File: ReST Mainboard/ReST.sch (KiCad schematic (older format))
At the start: 97 parts, among them IC1 AT24C128, P1 CONN_02X08, P10 CONN_01X04, P11 CONN_01X04, P12 CONN_02X04, P13 CONN_01X03, P14 CONN_02X03, P15 CONN_01X05, P16 CONN_01X03, P17 CONN_01X04, P18 CONN_02X04, P19 CONN_01X04, P2 CONN_02X08, P20 CONN_02X04, P21 CONN_02X04, P22 CONN_01X03, P23 SCREW_01X03, P24 CONN_01X03, P25 SCREW_01X03, P26 CONN_01X03, P27 SCREW_01X03, P28 CONN_01X03, P29 SCREW_01X03, P3 CONN_02X07, P30 CONN_01X03, P31 SCREW_01X03, P32 CONN_01X03, P33 SCREW_01X03, P34 CONN_01X03, P35 SCREW_01X04, P36 SCREW_01X04, P37 SCREW_01X04, P38 SCREW_01X04, P39 CONN_02X04, P4 CONN_02X10, P40 CONN_01X04, P41 CONN_01X04, P42 CONN_01X04, P43 CONN_02X03, P44 CONN_02X03, P45 CONN_02X03, P46 CONN_02X03, P5 USB_OTG, P6 CONN_02X05, P7 CONN_02X05, P8 CONN_01X09, P9 CONN_01X02, SW1 SW-SPST-NO, U1 STM32F103VE, U2 USBLC6-2, U3 L7805ACD2T-TR, U4 LM2574N-ADJ, U5 POLOLU_A4988, U6 POLOLU_A4988, U7 POLOLU_A4988, U8 POLOLU_A4988, X1 8MHZ RESONATOR

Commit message: Added BOM and changed Oscillator to Crystal
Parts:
- removed R4: 47R, Resistors_SMD:R_0805_HandSoldering, symbol R_Small
- removed X1: 8MHZ RESONATOR, ReST-Library:SMD-3P, symbol CRYSTAL_SMD
- added C24, C25: 30pF, Resistors_SMD:R_0805_HandSoldering, symbol C_Small
- added X1: Crystal_Small, Crystals:Crystal_HC49-SD_SMD, symbol Crystal_Small
- C8: footprint ok-polcaps-panasonic:CP-PANASONIC-SMT_C -> Capacitors_SMD:C_0805_HandSoldering
- C9: value 10nF -> 100nF
- L1: footprint ok-smd-generic:1206 -> Capacitors_SMD:C_0805_HandSoldering
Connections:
- wire segments 454 -> 447
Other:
- moved on the sheet: C8, C9, L1

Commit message: Removed unnecessary Libs and finished SD Card Module
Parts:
- U1: footprint ok-ic-smd:LQFP100-14x14 -> Housings_QFP:TQFP-100_14x14mm_Pitch0.5mm
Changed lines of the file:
@@
 F 0 "U1" H 2150 9550 50  0000 C CNN
 F 1 "STM32F103VE" H 4650 3950 50  0000 C CNN
-F 2 "ok-ic-smd:LQFP100-14x14" H 3500 6750 50  0001 C CNN
+F 2 "Housings_QFP:TQFP-100_14x14mm_Pitch0.5mm" H 3500 6750 50  0001 C CNN
 F 3 "" H 3500 7900 50  0000 C CNN
 	1    3500 6750

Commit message: Finally removed all unnecessary Libs and added Heatsink for 5V Regulator
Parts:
- C10: footprint ok-polcaps-panasonic:CP-PANASONIC-SMT_C -> ReST-Library:CP-PANASONIC-SMT_C
- C11, C12, C13: footprint ok-polcaps-panasonic:CP-PANASONIC-SMT_D -> ReST-Library:CP-PANASONIC-SMT_D
- C20, C21, C22, C23: footprint ok-polcaps-panasonic:CP-PANASONIC-SMT_D8 -> ReST-Library:CP-PANASONIC-SMT_D8
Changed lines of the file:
@@
 LIBS:dc-dc
 LIBS:diode
-LIBS:dp_devices
 LIBS:elec-unifil
 LIBS:ESD_Protection
@@
 LIBS:nordicsemi
 LIBS:nxp_armmcu
-LIBS:ok-74logic
-LIBS:ok-con-generic
-LIBS:ok-diodes
-LIBS:ok-generic
-LIBS:ok-ic-analog
-LIBS:ok-ic-atmel
-LIBS:ok-ic-com
-LIBS:ok-ic-memory
-LIBS:ok-ic-power
-LIBS:ok-ic-special
-LIBS:ok-ic-stm32
-LIBS:ok-jacks
-LIBS:ok-opto
-LIBS:ok-power
-LIBS:ok-relay
-LIBS:ok-switches
-LIBS:ok-transformers
-LIBS:ok-transistors
 LIBS:onsemi
 LIBS:Oscillators
-LIBS:pololu_a4988
 LIBS:Power_Management
 LIBS:powerint
@@
 LIBS:ReST-cache
 LIBS:STM32F103ZET6
-LIBS:small_rack-cache
 EELAYER 25 0
 EELAYER END
@@
 F 0 "C20" H 11760 3520 50  0000 L CNN
 F 1 "100uF" H 11760 3370 50  0000 L CNN
-F 2 "ok-polcaps-panasonic:CP-PANASONIC-SMT_D8" H 11750 3450 50  0001 C CNN
+F 2 "ReST-Library:CP-PANASONIC-SMT_D8" H 11750 3450 50  0001 C CNN
 F 3 "" H 11750 3450 50  0000 C CNN
 	1    11750 3450
@@
 F 0 "C21" H 11760 5520 50  0000 L CNN
 F 1 "100uF" H 11760 5370 50  0000 L CNN
-F 2 "ok-polcaps-panasonic:CP-PANASONIC-SMT_D8" H 11750 5450 50  0001 C CNN
+F 2 "ReST-Library:CP-PANASONIC-SMT_D8" H 11750 5450 50  0001 C CNN
 F 3 "" H 11750 5450 50  0000 C CNN
 	1    11750 5450
@@
 F 0 "C22" H 11810 9120 50  0000 L CNN
 F 1 "100uF" H 11810 8970 50  0000 L CNN
-F 2 "ok-polcaps-panasonic:CP-PANASONIC-SMT_D8" H 11800 9050 50  0001 C CNN
+F 2 "ReST-Library:CP-PANASONIC-SMT_D8" H 11800 9050 50  0001 C CNN
 F 3 "" H 11800 9050 50  0000 C CNN
 	1    11800 9050
@@
 F 0 "C23" H 11810 7420 50  0000 L CNN
 F 1 "100uF" H 11810 7270 50  0000 L CNN
-F 2 "ok-polcaps-panasonic:CP-PANASONIC-SMT_D8" H 11800 7350 50  0001 C CNN
+F 2 "ReST-Library:CP-PANASONIC-SMT_D8" H 11800 7350 50  0001 C CNN
 F 3 "" H 11800 7350 50  0000 C CNN
 	1    11800 7350
@@
 F 0 "C10" H 960 1770 50  0000 L CNN
 F 1 "10uF" H 960 1620 50  0000 L CNN
-F 2 "ok-polcaps-panasonic:CP-PANASONIC-SMT_C" H 950 1700 50  0001 C CNN
+F 2 "ReST-Library:CP-PANASONIC-SMT_C" H 950 1700 50  0001 C CNN
 F 3 "" H 950 1700 50  0000 C CNN
 	1    950  1700
@@
 F 0 "C11" H 1960 1770 50  0000 L CNN
 F 1 "22uF" H 1960 1620 50  0000 L CNN
-F 2 "ok-polcaps-panasonic:CP-PANASONIC-SMT_D" H 1950 1700 50  0001 C CNN
+F 2 "ReST-Library:CP-PANASONIC-SMT_D" H 1950 1700 50  0001 C CNN
 F 3 "" H 1950 1700 50  0000 C CNN
 	1    1950 1700
@@
 F 0 "C12" H 2560 1520 50  0000 L CNN
 F 1 "22uF" H 2560 1370 50  0000 L CNN
-F 2 "ok-polcaps-panasonic:CP-PANASONIC-SMT_D" H 2550 1450 50  0001 C CNN
+F 2 "ReST-Library:CP-PANASONIC-SMT_D" H 2550 1450 50  0001 C CNN
 F 3 "" H 2550 1450 50  0000 C CNN
 	1    2550 1450
@@
 F 0 "C13" H 4560 1770 50  0000 L CNN
 F 1 "220uF" H 4560 1620 50  0000 L CNN
-F 2 "ok-polcaps-panasonic:CP-PANASONIC-SMT_D" H 4550 1700 50  0001 C CNN
+F 2 "ReST-Library:CP-PANASONIC-SMT_D" H 4550 1700 50  0001 C CNN
 F 3 "" H 4550 1700 50  0000 C CNN
 	1    4550 1700

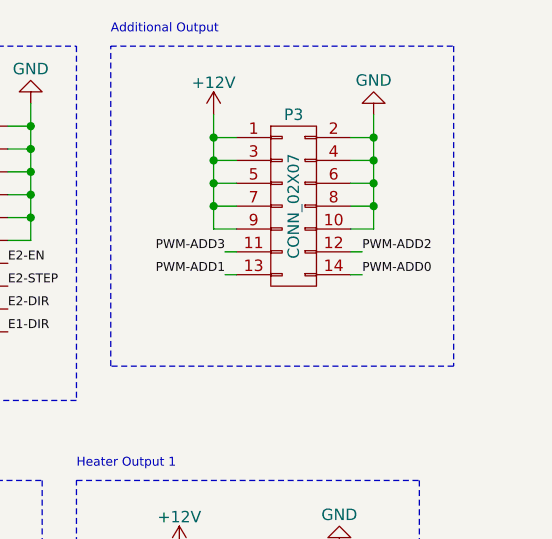
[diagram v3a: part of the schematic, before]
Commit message: Added IRLML2502 Module and added Ground vias everywhere
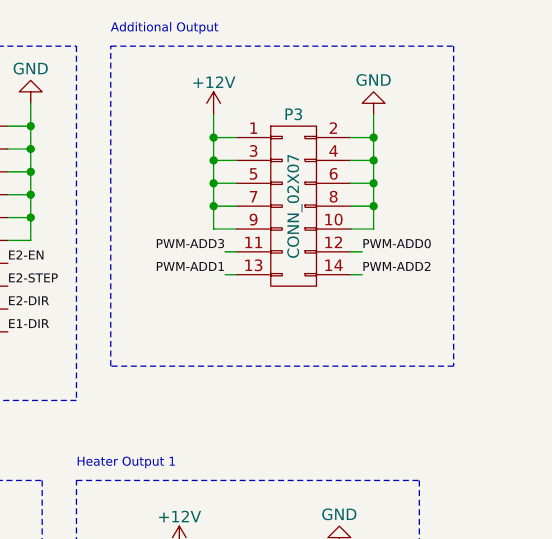
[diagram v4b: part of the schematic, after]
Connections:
- net PWM-ADD0: now also P3.12 (P12); no longer P3.14 (P14)
- net PWM-ADD2: now also P3.14 (P14); no longer P3.12 (P12)
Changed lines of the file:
@@
 Text Label 5700 6750 0    39   ~ 0
 I2C-SDA
+Text Label 15200 1550 0    39   ~ 0
+PWM-ADD0
 Text Label 15200 1650 0    39   ~ 0
-PWM-ADD0
-Text Label 15200 1550 0    39   ~ 0
 PWM-ADD2
 Text Label 14600 1550 2    39   ~ 0

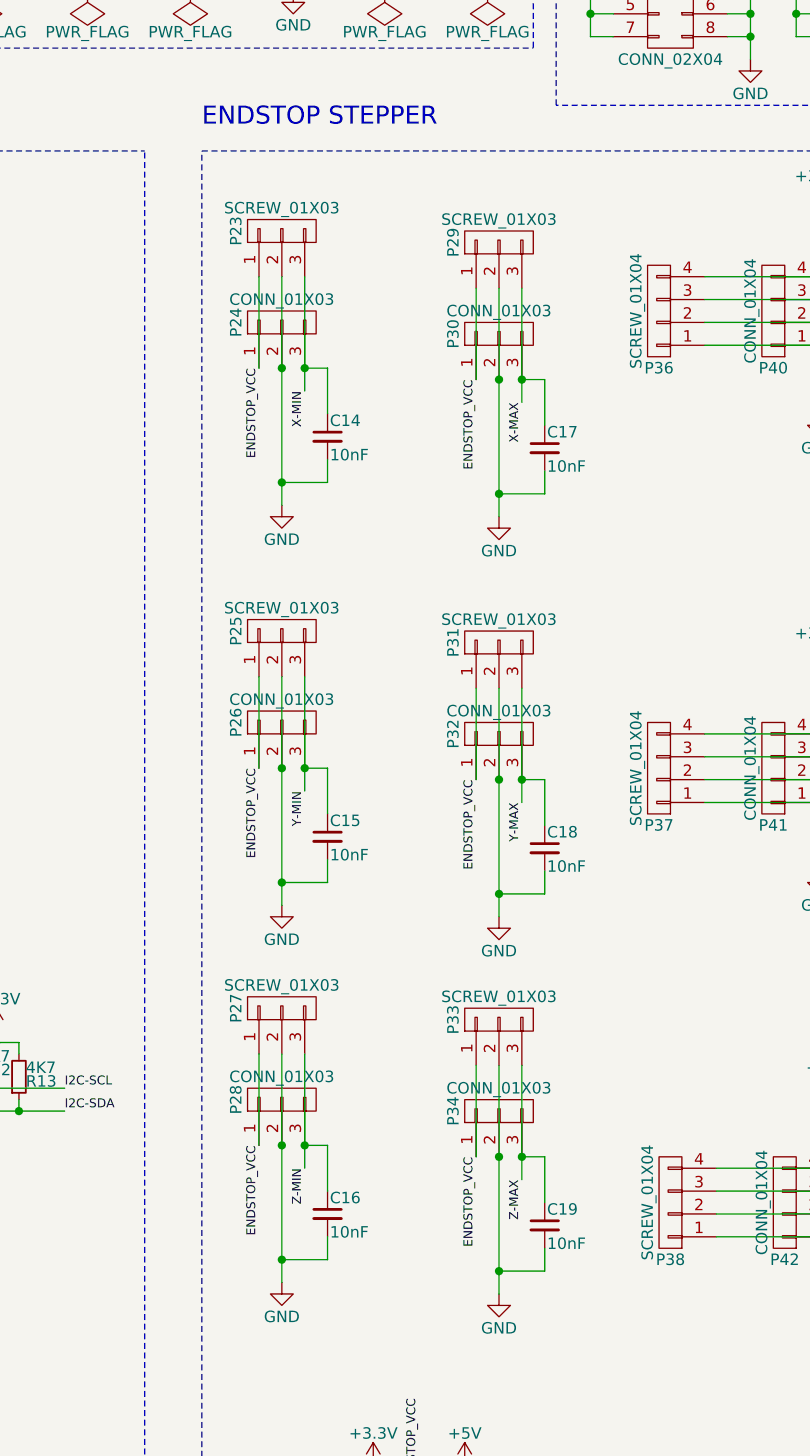
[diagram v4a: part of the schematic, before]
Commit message: Added BOM for all Items + suggested Links
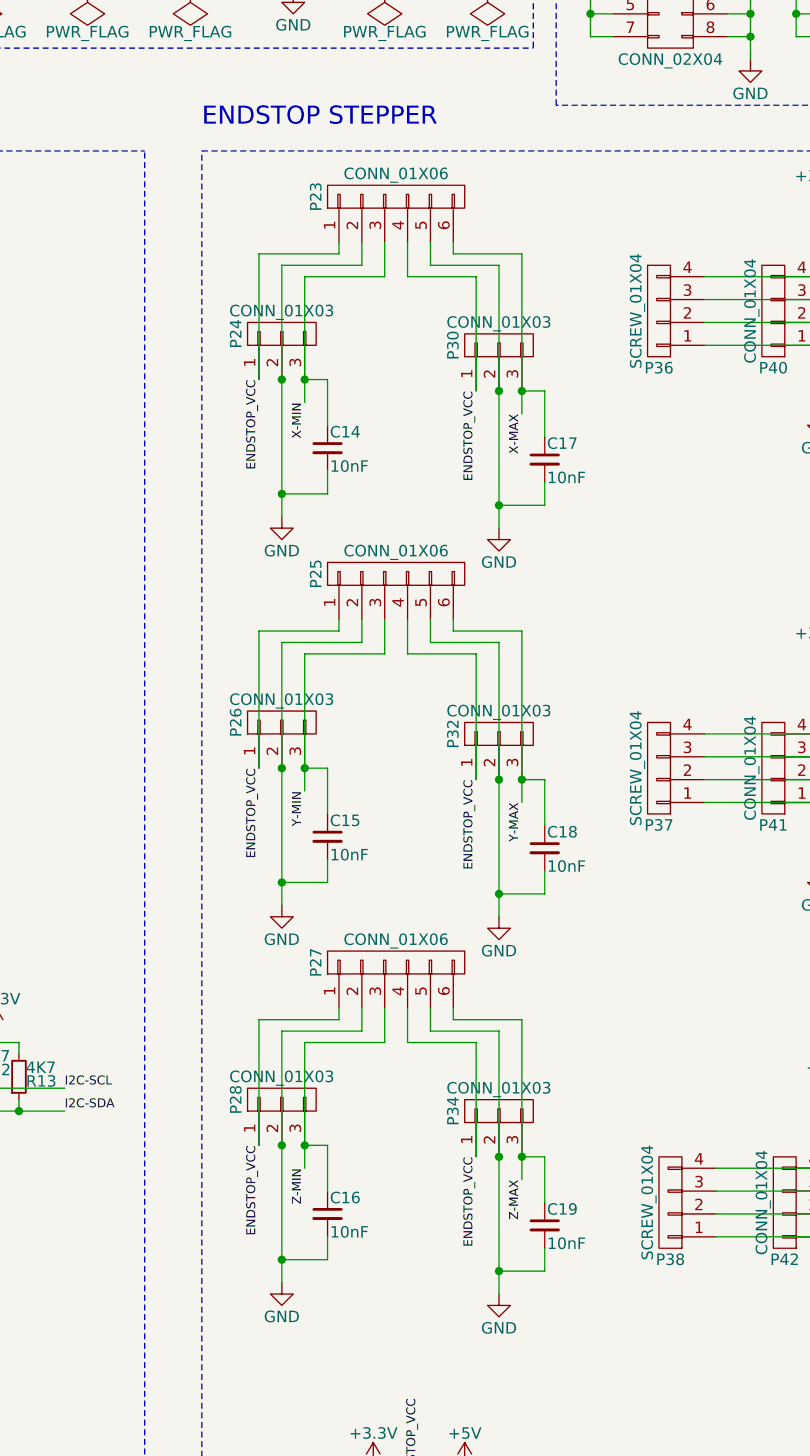
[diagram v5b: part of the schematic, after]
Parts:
- removed P23, P25, P27, P29, P31, P33: SCREW_01X03, 2:mpt_0,5%2f3-2,54, symbol CONN_01X03
- added P23, P25, P27: CONN_01X06, 2:mpt_0,5%2f6-2,54, symbol CONN_01X06
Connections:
- net ENDSTOP_VCC: now also P23.1 (P1), P23.4 (P4), P25.1 (P1), P25.4 (P4), P27.1 (P1), P27.4 (P4)
- net GND: now also P23.2 (P2), P23.5 (P5), P25.2 (P2), P25.5 (P5), P27.2 (P2), P27.5 (P5)
- net X-MAX: now also P23.6 (P6)
- net X-MIN: now also P23.3 (P3)
- net Y-MAX: now also P25.6 (P6)
- net Y-MIN: now also P25.3 (P3)
- net Z-MAX: now also P27.6 (P6)
- net Z-MIN: now also P27.3 (P3)
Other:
- moved on the sheet: C14, C17, P24, P30

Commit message: Added relative paths and linked footprint to a extra repo
hope i finally fixed the problem with missing libs. will try to add the
3d views, too
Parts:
- U1: footprint Housings_QFP:TQFP-100_14x14mm_Pitch0.5mm -> ReST-Library:LQFP100-14x14
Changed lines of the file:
@@
 LIBS:Zilog
 LIBS:ReST-cache
-LIBS:STM32F103ZET6
 EELAYER 25 0
 EELAYER END
@@
 F 0 "U1" H 2150 9550 50  0000 C CNN
 F 1 "STM32F103VE" H 4650 3950 50  0000 C CNN
-F 2 "Housings_QFP:TQFP-100_14x14mm_Pitch0.5mm" H 3500 6750 50  0001 C CNN
+F 2 "ReST-Library:LQFP100-14x14" H 3500 6750 50  0001 C CNN
 F 3 "" H 3500 7900 50  0000 C CNN
 	1    3500 6750

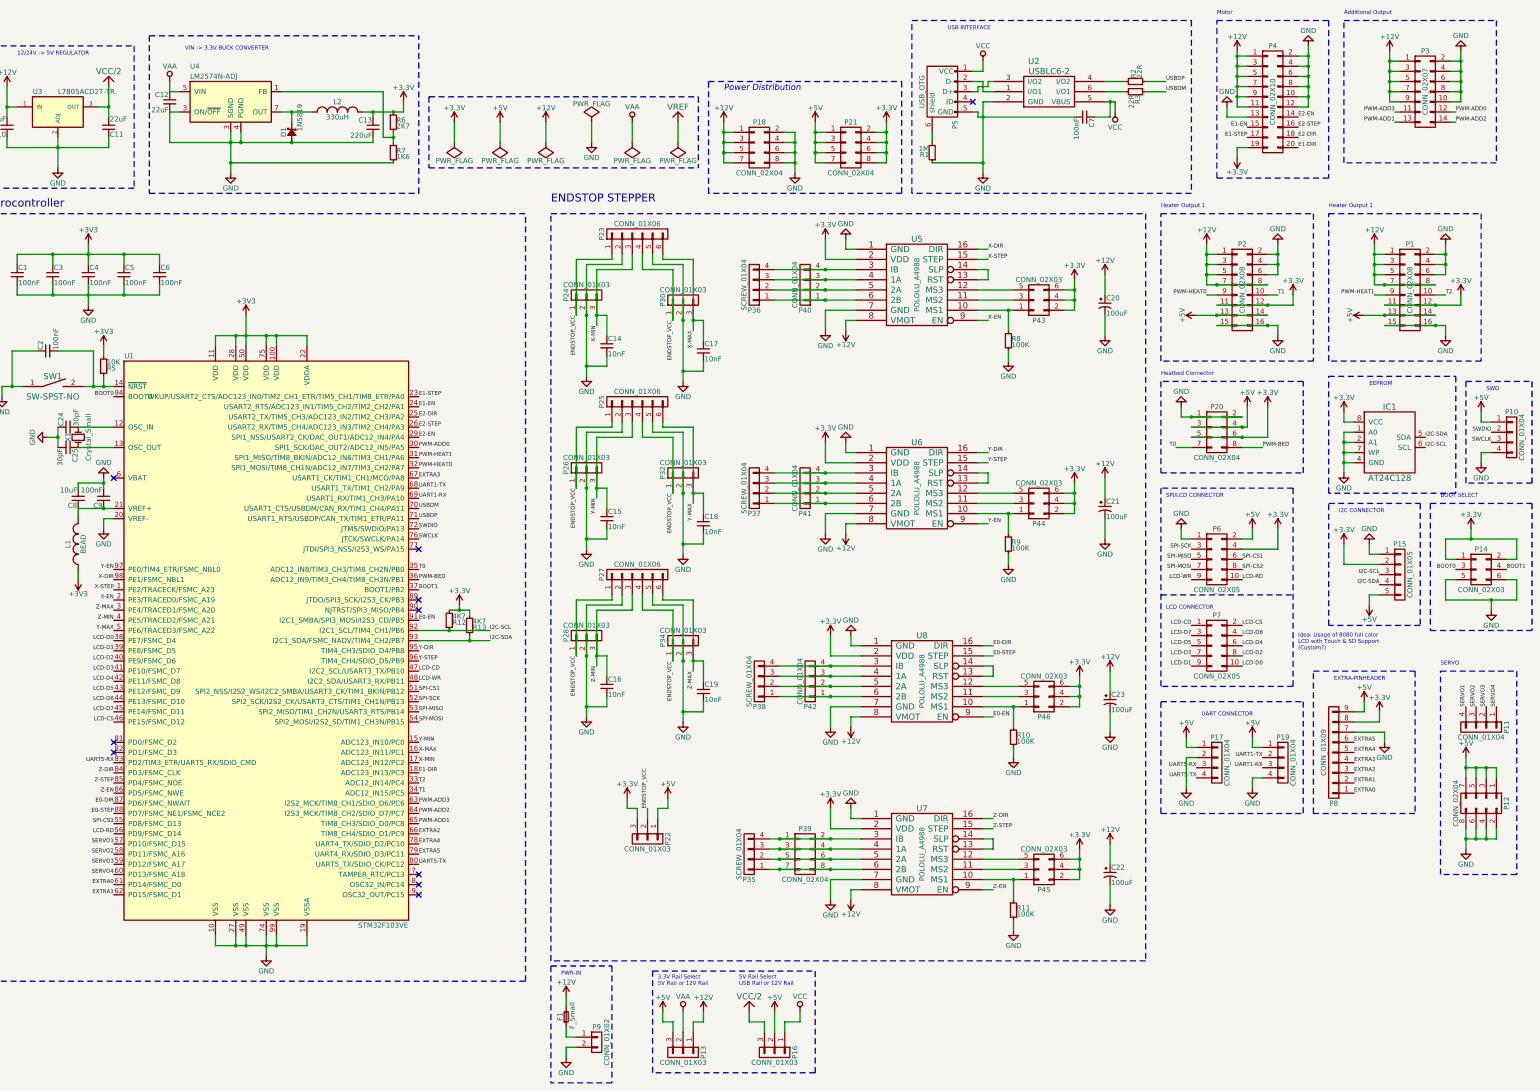
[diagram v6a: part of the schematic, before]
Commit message: Reworked Modules to sit ontop of the mainboard
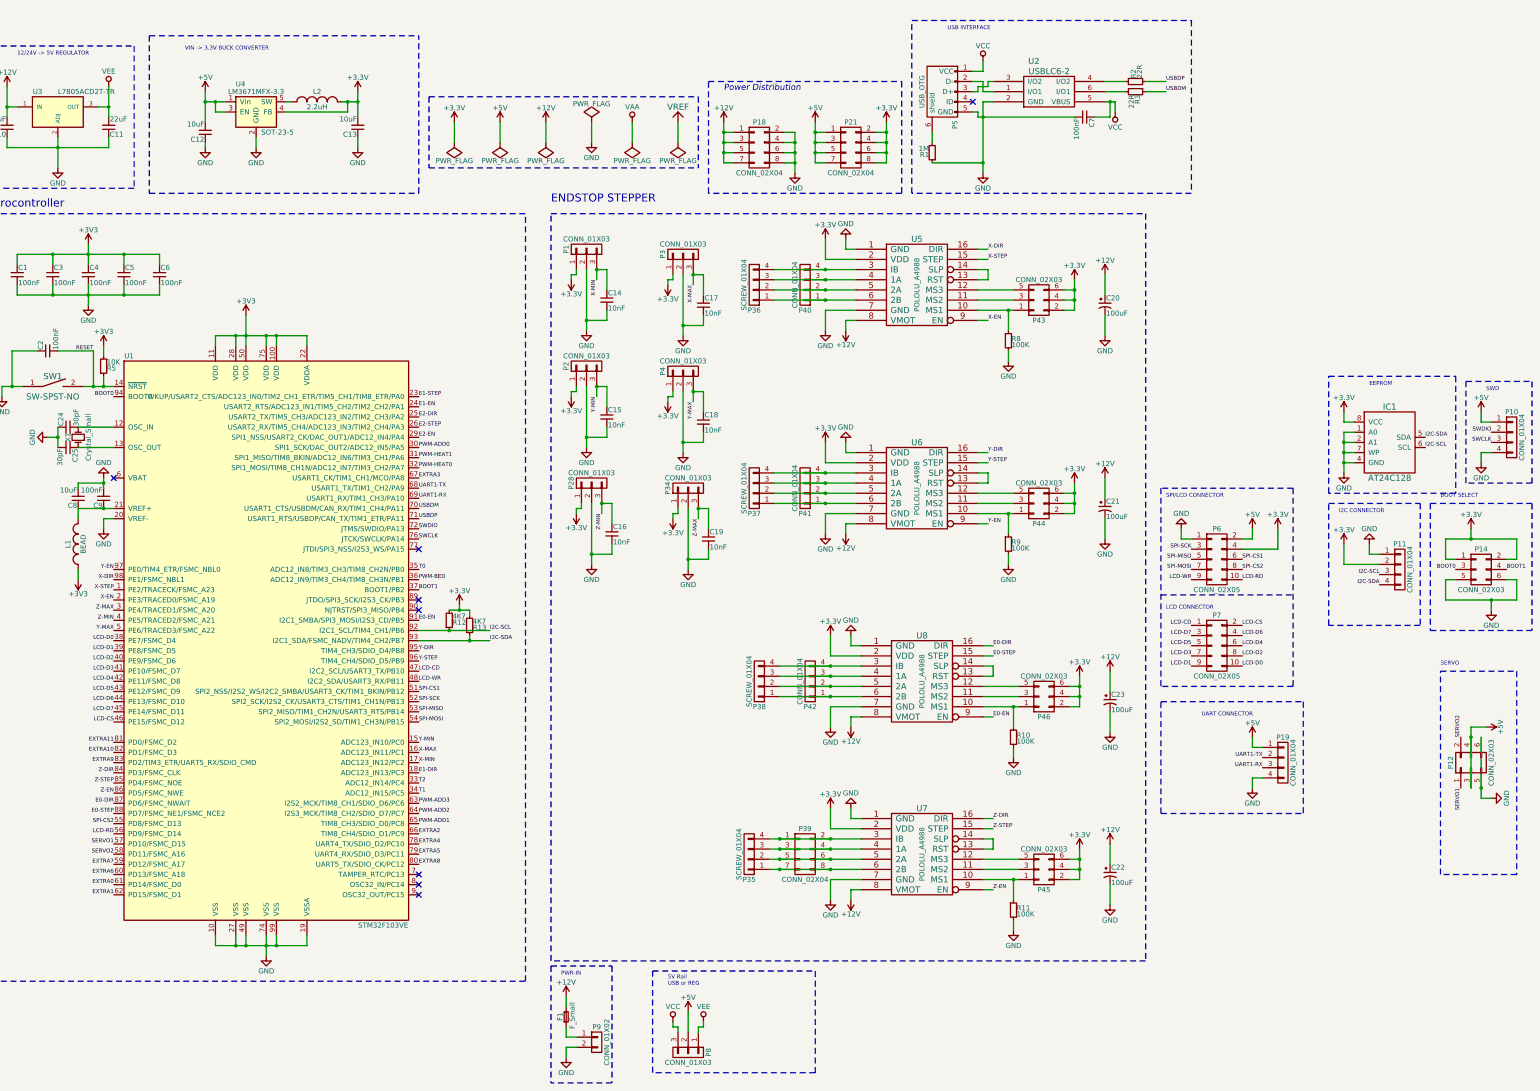
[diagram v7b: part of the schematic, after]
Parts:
- removed D1: 1N5819, ReST-Library:DO-214AC(SMA), symbol D_Schottky_Small
- removed P1, P2: CONN_02X08, Pin_Headers:Pin_Header_Angled_2x08, symbol CONN_02X08
- removed P12: CONN_02X04, Pin_Headers:Pin_Header_Straight_2x04, symbol CONN_02X04
- removed P13, P16, P22, P24, P26, P30, P32: CONN_01X03, Pin_Headers:Pin_Header_Straight_1x03, symbol CONN_01X03
- removed P15: CONN_01X05, Pin_Headers:Pin_Header_Straight_1x05, symbol CONN_01X05
- removed P17: CONN_01X04, Pin_Headers:Pin_Header_Straight_1x04, symbol CONN_01X04
- removed P20: CONN_02X04, Pin_Headers:Pin_Header_Angled_2x04, symbol CONN_02X04
- removed P23, P25, P27: CONN_01X06, 2:mpt_0,5%2f6-2,54, symbol CONN_01X06
- removed P3: CONN_02X07, Pin_Headers:Pin_Header_Angled_2x07, symbol CONN_02X07
- removed P4: CONN_02X10, Pin_Headers:Pin_Header_Angled_2x10, symbol CONN_02X10
- removed P8: CONN_01X09, Pin_Headers:Pin_Header_Straight_1x09, symbol CONN_01X09
- removed R6: 2K7, Resistors_SMD:R_0805_HandSoldering, symbol R_Small
- removed R7: 1K6, Resistors_SMD:R_0805_HandSoldering, symbol R_Small
- removed U4: LM2574N-ADJ, Housings_DIP:DIP-8_W7.62mm_LongPads, symbol LM2574N-ADJ
- added P1, P2, P3, P4: CONN_01X03, Pin_Headers:Pin_Header_Straight_1x03, symbol CONN_01X03
- added P12: CONN_02X03, Pin_Headers:Pin_Header_Straight_2x03, symbol CONN_02X03
- added P8: CONN_01X03, symbol CONN_01X03
- added U4: LM3671MFX-3.3, SOT-23-5, symbol LM3670MF
- C12: value 22uF -> 10uF; footprint ReST-Library:CP-PANASONIC-SMT_D -> Capacitors_SMD:C_0805_HandSoldering
- C13: value 220uF -> 10uF; footprint ReST-Library:CP-PANASONIC-SMT_D -> Capacitors_SMD:C_0805_HandSoldering
- L2: value 330uH -> 2.2uH; footprint Inductors:SELF-WE-PD-XXL -> (none)
- X1: footprint Crystals:Crystal_HC49-SD_SMD -> ReST-Library:2P-5032
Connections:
- net ENDSTOP_VCC is gone; now on net +3V3: P28.1 (P1), P34.1 (P1)
- net +3V3: now also C13.2, P11.2 (P2), P1.1 (P1), P2.1 (P1), P3.1 (P1), P4.1 (P1), U4.4 (FB); no longer C13.1
- net +5V: now also C12.2, P12.3 (P3), P12.4 (P4), P8.2 (P2), U4.1 (Vin), U4.3 (EN)
- net GND: now also C12.1, C13.1, P11.1 (P1), P1.2 (P2), P12.5 (P5), P12.6 (P6), P2.2 (P2), P3.2 (P2), P4.2 (P2), U4.2 (GND); no longer C12.2, C13.2
- net I2C-SCL: now also P11.3 (P3)
- net I2C-SDA: now also P11.4 (P4)
- net SERVO1: now also P12.1 (P1); no longer P11.4 (P4)
- net SERVO2: now also P12.2 (P2); no longer P11.3 (P3)
- net VAA: no longer C12.1
- net VCC: now also P8.3 (P3)
- net X-MAX: now also P3.3 (P3)
- net X-MIN: now also P1.3 (P3)
- net Y-MAX: now also P4.3 (P3)
- net Y-MIN: now also P2.3 (P3)
- net RESET: now reaches C2.2, R5.1, SW1.2, U1.14 (~NRST)
- net EXTRA11: now reaches U1.81 (PD0/FSMC_D2)
- net EXTRA10: now reaches U1.82 (PD1/FSMC_D3)
- net at L2.1: now also U4.5 (SW)
- net SERVO3 renamed EXTRA7
- net EXTRA7: no longer P11.2 (P2)
- net SERVO4 renamed EXTRA6
- net EXTRA6: no longer P11.1 (P1)
- net UART5-RX renamed EXTRA9
- net UART5-TX renamed EXTRA8
- net VCC/2 renamed VEE
- net VEE: now also P8.1 (P1)
- no-connect marks 10 -> 8
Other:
- note added: "5V Rail\nUSB or REG"
- note removed: "3.3V Rail Select\n5V Rail or 12V Rail"
- note removed: "5V Rail Select\nUSB Rail or 12V Rail"
- note removed: "Additional Output"
- note removed: "EXTRA-PINHEADER"
- note removed: "Heatbed Connector"
- note removed: "Heater Output 1"
- note removed: "Idea: Usage of 8080 full color \nLCD with Touch & SD Support\n(Custom?)"
- note removed: "Motor"
- moved on the sheet: C16, C19, P28, P34
